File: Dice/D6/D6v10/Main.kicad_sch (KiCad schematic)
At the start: 29 parts, among them J1 Conn_01x14, J2 Conn_01x04, J4 DNP, U1 N52810_QFN32, U2 SC7A20HTR, U5 BL24C02F-NTRC, U8 SL1605, Y1 32MHz 40ppm

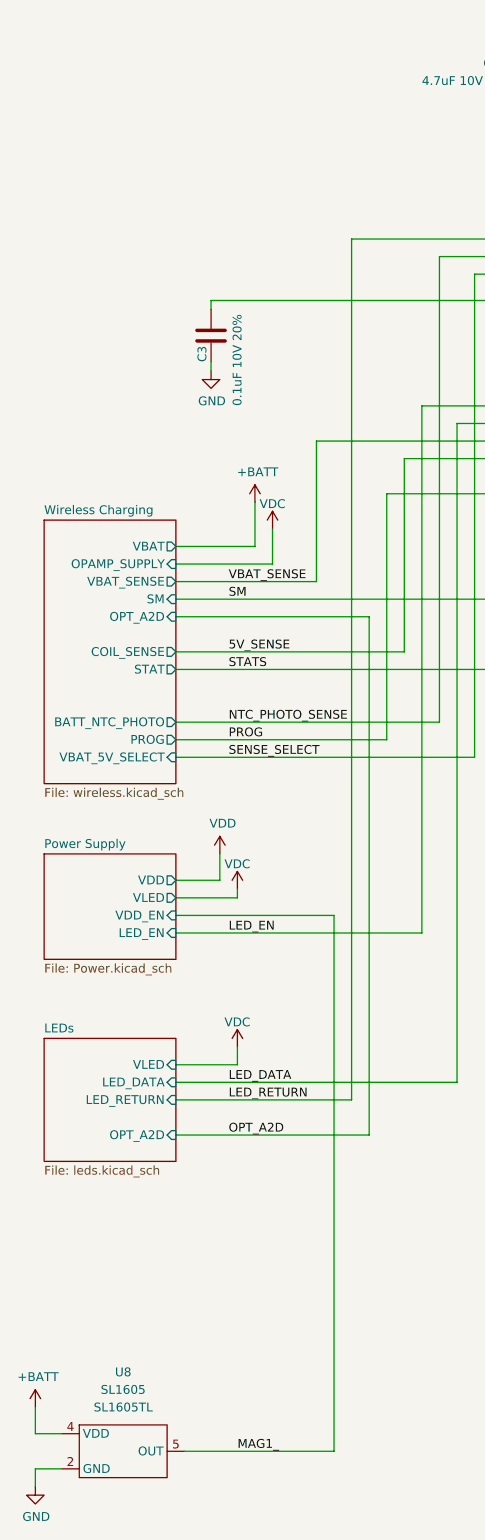
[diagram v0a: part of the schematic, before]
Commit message: Updated schematic Titles in D20V17 and likes, added 12mm D6 and Charging Jig
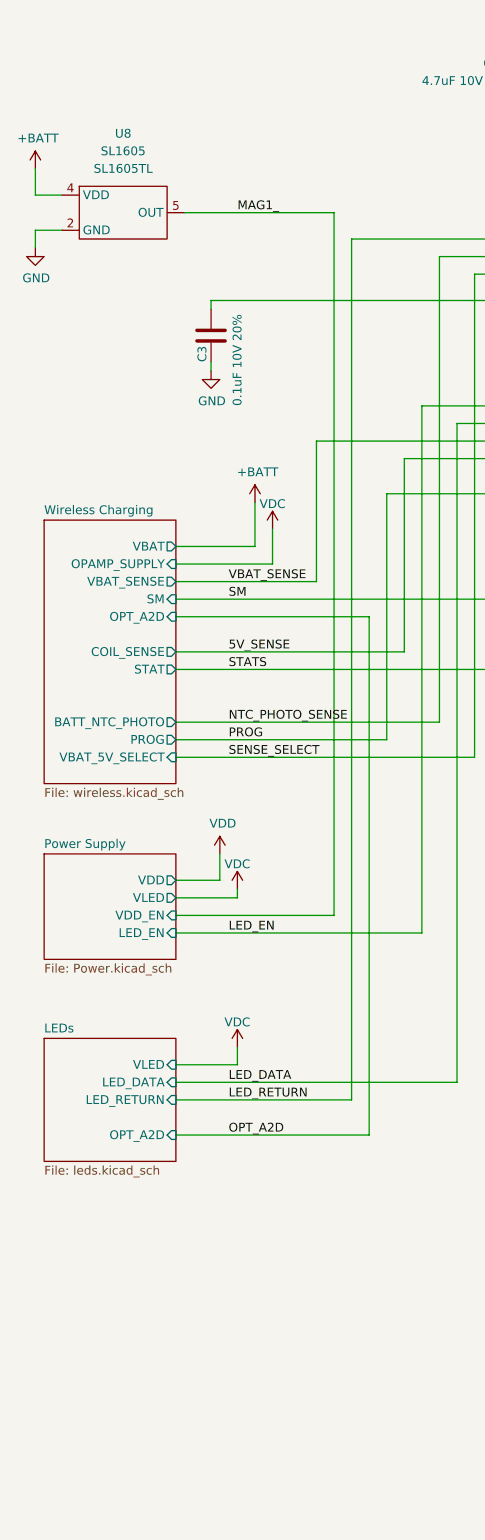
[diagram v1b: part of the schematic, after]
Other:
- title: Pixels D20 Schematic, Main -> Pixels D6V10 Schematic, Main
- moved on the sheet: U8
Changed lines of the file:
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@@
 	(paper "A4")
 	(title_block
-		(title "Pixels D20 Schematic, Main")
-		(date "2022-08-26")
+		(title "Pixels D6V10 Schematic, Main")
+		(date "2025-10-10")
 		(rev "13")
 		(company "Systemic Games, LLC")
@@
 	(wire
 		(pts
-			(xy 40.64 227.33) (xy 62.23 227.33)
+			(xy 40.64 48.26) (xy 62.23 48.26)
 		)
 		(stroke
@@
 	(wire
 		(pts
-			(xy 19.05 220.98) (xy 19.05 224.79)
+			(xy 19.05 41.91) (xy 19.05 45.72)
 		)
 		(stroke
@@
 	(wire
 		(pts
-			(xy 62.23 149.86) (xy 62.23 227.33)
+			(xy 62.23 149.86) (xy 62.23 48.26)
 		)
 		(stroke
@@
 	(wire
 		(pts
-			(xy 22.86 229.87) (xy 19.05 229.87)
+			(xy 22.86 50.8) (xy 19.05 50.8)
 		)
 		(stroke
@@
 	(wire
 		(pts
-			(xy 19.05 229.87) (xy 19.05 232.41)
+			(xy 19.05 50.8) (xy 19.05 53.34)
 		)
 		(stroke
@@
 	(wire
 		(pts
-			(xy 19.05 224.79) (xy 22.86 224.79)
+			(xy 19.05 45.72) (xy 22.86 45.72)
 		)
 		(stroke
@@
 	)
 	(label "MAG1_"
-		(at 48.26 227.33 0)
+		(at 48.26 48.26 0)
 		(effects
 			(font
@@
 	(symbol
 		(lib_id "power:GND")
-		(at 19.05 232.41 0)
+		(at 19.05 53.34 0)
 		(unit 1)
 		(exclude_from_sim no)
@@
 		(dnp no)
 		(property "Reference" "#PWR045"
-			(at 19.05 238.76 0)
+			(at 19.05 59.69 0)
 			(effects
 				(font
@@
 		)
 		(property "Value" "GND"
-			(at 19.177 236.8042 0)
+			(at 19.177 57.7342 0)
 			(effects
 				(font
@@
 		)
 		(property "Footprint" ""
-			(at 19.05 232.41 0)
+			(at 19.05 53.34 0)
 			(effects
 				(font
@@
 		)
 		(property "Datasheet" ""
-			(at 19.05 232.41 0)
+			(at 19.05 53.34 0)
 			(effects
 				(font
@@
 		)
 		(property "Description" ""
-			(at 19.05 232.41 0)
+			(at 19.05 53.34 0)
 			(effects
 				(font
@@
 	(symbol
 		(lib_id "power:+BATT")
-		(at 19.05 220.98 0)
+		(at 19.05 41.91 0)
 		(unit 1)
 		(exclude_from_sim no)
@@
 		(dnp no)
 		(property "Reference" "#PWR017"
-			(at 19.05 224.79 0)
+			(at 19.05 45.72 0)
 			(effects
 				(font
@@
 		)
 		(property "Value" "+BATT"
-			(at 19.431 216.5858 0)
+			(at 19.431 37.5158 0)
 			(effects
 				(font
@@
 		)
 		(property "Footprint" ""
-			(at 19.05 220.98 0)
+			(at 19.05 41.91 0)
 			(effects
 				(font
@@
 		)
 		(property "Datasheet" ""
-			(at 19.05 220.98 0)
+			(at 19.05 41.91 0)
 			(effects
 				(font
@@
 		)
 		(property "Description" ""
-			(at 19.05 220.98 0)
+			(at 19.05 41.91 0)
 			(effects
 				(font
@@
 	(symbol
 		(lib_id "Pixels-dice:SL1605")
-		(at 31.75 227.33 0)
+		(at 31.75 48.26 0)
 		(unit 1)
 		(exclude_from_sim no)
@@
 		(fields_autoplaced yes)
 		(property "Reference" "U8"
-			(at 31.75 215.9 0)
+			(at 31.75 36.83 0)
 			(effects
 				(font
@@
 		)
 		(property "Value" "SL1605"
-			(at 31.75 218.44 0)
+			(at 31.75 39.37 0)
 			(effects
 				(font
@@
 		)
 		(property "Footprint" "Package_TO_SOT_SMD:SOT-553"
-			(at 31.75 227.33 0)
+			(at 31.75 48.26 0)
 			(effects
 				(font
@@
 		)
 		(property "Datasheet" ""
-			(at 31.75 227.33 0)
+			(at 31.75 48.26 0)
 			(effects
 				(font
@@
 		)
 		(property "Description" ""
-			(at 31.75 227.33 0)
+			(at 31.75 48.26 0)
 			(effects
 				(font
@@
 		)
 		(property "Manufacturer" "Slkor(SLKORMICRO Elec.)"
-			(at 31.75 227.33 0)
+			(at 31.75 48.26 0)
 			(effects
 				(font
@@
 		)
 		(property "Part Number" "SL1605TL"
-			(at 31.75 220.98 0)
+			(at 31.75 41.91 0)
 			(effects
 				(font
@@
 		)
 		(property "LCSC Part #" "C2826474"
-			(at 31.75 227.33 0)
+			(at 31.75 48.26 0)
 			(effects
 				(font
